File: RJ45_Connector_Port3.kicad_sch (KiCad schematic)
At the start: 8 parts, among them J1 0826-1X4T-43-F

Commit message: Adding page title, and confidential for now
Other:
- title: (none) -> RJ45 Connector Port 3
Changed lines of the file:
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@@
 	(paper "A4")
 	(title_block
+		(title "RJ45 Connector Port 3")
 		(date "2025-12-21")
 		(rev "Rev. A")
 		(company "Kebag-Logic <contact@kebag-logic.com>")
+		(comment 1 "Confidential")
 	)
 	(junction

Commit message: fixes ERC errors in DC/DC converters
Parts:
- C15, C16, C17, C2: footprint Capacitor_SMD:C_0201_0603Metric -> KL_Footprints:C_0603; Dielectric X7R -> (none); Farnell 4539043 -> (none); Package_in_inch 0603 -> (none); Tolerance_in_pct 10 -> (none)
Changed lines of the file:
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@@
 		(dnp no)
 		(property "Reference" "C16"
-			(at 80.01 58.928 90)
-			(effects
-				(font
-					(size 1.27 1.27)
-				)
+			(at 77.47 61.595 0)
+			(effects
+				(font
+					(size 1.27 1.27)
+				)
+				(justify left)
 			)
 		)
 		(property "Value" "100n"
-			(at 80.01 65.786 90)
-			(effects
-				(font
-					(size 1.27 1.27)
-				)
-			)
-		)
-		(property "Footprint" "Capacitor_SMD:C_0201_0603Metric"
+			(at 82.55 61.595 0)
+			(effects
+				(font
+					(size 1.27 1.27)
+				)
+				(justify left)
+			)
+		)
+		(property "Footprint" "KL_Footprints:C_0603"
 			(at 83.82 61.2648 0)
 			(effects
@@
 		)
 		(property "LCSC" "C1591"
-			(at 80.01 62.23 0)
-			(effects
-				(font
-					(size 1.27 1.27)
-				)
-				(hide yes)
-			)
-		)
-		(property "Tolerance_in_pct" "10"
-			(at 80.01 62.23 0)
-			(effects
-				(font
-					(size 1.27 1.27)
-				)
-				(hide yes)
-			)
-		)
-		(property "Dielectric" "X7R"
-			(at 80.01 62.23 0)
-			(effects
-				(font
-					(size 1.27 1.27)
-				)
-				(hide yes)
-			)
-		)
-		(property "Package_in_inch" "0603"
-			(at 80.01 62.23 0)
-			(effects
-				(font
-					(size 1.27 1.27)
-				)
-				(hide yes)
-			)
-		)
-		(property "Farnell" "4539043"
 			(at 80.01 62.23 0)
 			(effects
@@
 		(dnp no)
 		(property "Reference" "C15"
-			(at 80.01 48.514 90)
-			(effects
-				(font
-					(size 1.27 1.27)
-				)
+			(at 77.47 51.435 0)
+			(effects
+				(font
+					(size 1.27 1.27)
+				)
+				(justify left)
 			)
 		)
 		(property "Value" "100n"
-			(at 80.01 55.626 90)
-			(effects
-				(font
-					(size 1.27 1.27)
-				)
-			)
-		)
-		(property "Footprint" "Capacitor_SMD:C_0201_0603Metric"
+			(at 82.55 51.435 0)
+			(effects
+				(font
+					(size 1.27 1.27)
+				)
+				(justify left)
+			)
+		)
+		(property "Footprint" "KL_Footprints:C_0603"
 			(at 83.82 51.1048 0)
 			(effects
@@
 		)
 		(property "LCSC" "C1591"
-			(at 80.01 52.07 0)
-			(effects
-				(font
-					(size 1.27 1.27)
-				)
-				(hide yes)
-			)
-		)
-		(property "Tolerance_in_pct" "10"
-			(at 80.01 52.07 0)
-			(effects
-				(font
-					(size 1.27 1.27)
-				)
-				(hide yes)
-			)
-		)
-		(property "Dielectric" "X7R"
-			(at 80.01 52.07 0)
-			(effects
-				(font
-					(size 1.27 1.27)
-				)
-				(hide yes)
-			)
-		)
-		(property "Package_in_inch" "0603"
-			(at 80.01 52.07 0)
-			(effects
-				(font
-					(size 1.27 1.27)
-				)
-				(hide yes)
-			)
-		)
-		(property "Farnell" "4539043"
 			(at 80.01 52.07 0)
 			(effects
@@
 		(dnp no)
 		(property "Reference" "C17"
-			(at 80.01 68.834 90)
-			(effects
-				(font
-					(size 1.27 1.27)
-				)
+			(at 77.47 71.755 0)
+			(effects
+				(font
+					(size 1.27 1.27)
+				)
+				(justify left)
 			)
 		)
 		(property "Value" "100n"
-			(at 80.01 75.946 90)
-			(effects
-				(font
-					(size 1.27 1.27)
-				)
-			)
-		)
-		(property "Footprint" "Capacitor_SMD:C_0201_0603Metric"
+			(at 82.55 71.755 0)
+			(effects
+				(font
+					(size 1.27 1.27)
+				)
+				(justify left)
+			)
+		)
+		(property "Footprint" "KL_Footprints:C_0603"
 			(at 83.82 71.4248 0)
 			(effects
@@
 		)
 		(property "LCSC" "C1591"
-			(at 80.01 72.39 0)
-			(effects
-				(font
-					(size 1.27 1.27)
-				)
-				(hide yes)
-			)
-		)
-		(property "Tolerance_in_pct" "10"
-			(at 80.01 72.39 0)
-			(effects
-				(font
-					(size 1.27 1.27)
-				)
-				(hide yes)
-			)
-		)
-		(property "Dielectric" "X7R"
-			(at 80.01 72.39 0)
-			(effects
-				(font
-					(size 1.27 1.27)
-				)
-				(hide yes)
-			)
-		)
-		(property "Package_in_inch" "0603"
-			(at 80.01 72.39 0)
-			(effects
-				(font
-					(size 1.27 1.27)
-				)
-				(hide yes)
-			)
-		)
-		(property "Farnell" "4539043"
 			(at 80.01 72.39 0)
 			(effects
@@
 		(dnp no)
 		(property "Reference" "C2"
-			(at 80.01 38.608 90)
-			(effects
-				(font
-					(size 1.27 1.27)
-				)
+			(at 77.47 41.275 0)
+			(effects
+				(font
+					(size 1.27 1.27)
+				)
+				(justify left)
 			)
 		)
 		(property "Value" "100n"
-			(at 80.01 45.212 90)
-			(effects
-				(font
-					(size 1.27 1.27)
-				)
-			)
-		)
-		(property "Footprint" "Capacitor_SMD:C_0201_0603Metric"
+			(at 82.55 41.275 0)
+			(effects
+				(font
+					(size 1.27 1.27)
+				)
+				(justify left)
+			)
+		)
+		(property "Footprint" "KL_Footprints:C_0603"
 			(at 83.82 40.9448 0)
 			(effects
@@
 			(at 80.01 41.91 0)
 			(effects
-				(font
-					(size 1.27 1.27)
-				)
-				(hide yes)
-			)
-		)
-		(property "Tolerance_in_pct" "10"
-			(at 80.01 41.91 0)
-			(effects
-				(font
-					(size 1.27 1.27)
-				)
-				(hide yes)
-			)
-		)
-		(property "Dielectric" "X7R"
-			(at 80.01 41.91 0)
-			(effects
-				(font
-					(size 1.27 1.27)
-				)
-				(hide yes)
-			)
-		)
-		(property "Package_in_inch" "0603"
-			(at 80.01 41.91 0)
-			(effects
-				(font
-					(size 1.27 1.27)
-				)
-				(hide yes)
-			)
-		)
-		(property "Farnell" "4539043"
-			(at 80.01 41.91 0)
-			(effects

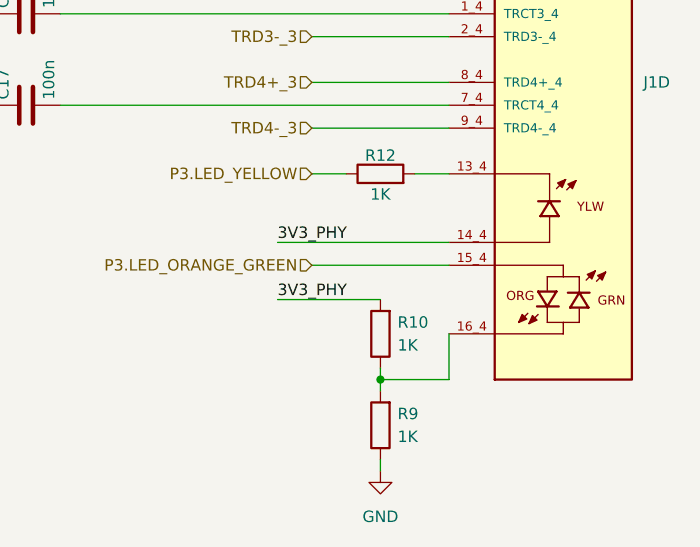
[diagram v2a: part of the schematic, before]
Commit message: updates components from my library misconfiguration. Refs: #1
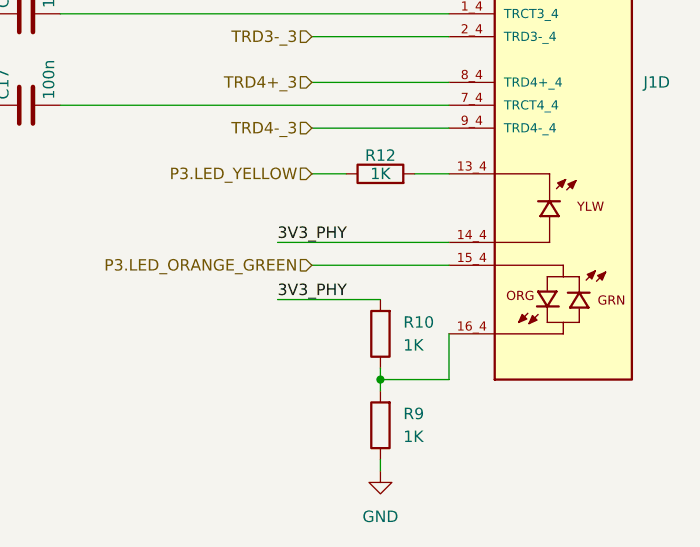
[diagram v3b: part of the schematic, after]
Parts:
- J1: footprint 0826-1X4T-43-F:BEL_0826-1X4T-43-F -> KL_Footprints:BEL_0826-1X4T-43-F
- R10, R12, R9: footprint KL_Footprints:C_0603 -> KL_Footprints:R_0603
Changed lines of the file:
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@@
 		(fields_autoplaced yes)
 		(property "Reference" "R10"
-			(at 121.285 96.5199 0)
+			(at 121.92 96.5199 0)
 			(effects
 				(font
@@
 		)
 		(property "Value" "1K"
-			(at 121.285 99.0599 0)
+			(at 121.92 99.0599 0)
 			(effects
 				(font
@@
 			)
 		)
-		(property "Footprint" "KL_Footprints:C_0603"
+		(property "Footprint" "KL_Footprints:R_0603"
 			(at 121.158 97.79 90)
 			(effects
@@
 			)
 		)
-		(property "Footprint" "0826-1X4T-43-F:BEL_0826-1X4T-43-F"
+		(property "Footprint" "KL_Footprints:BEL_0826-1X4T-43-F"
 			(at 139.7 69.85 0)
 			(effects
@@
 		(fields_autoplaced yes)
 		(property "Reference" "R9"
-			(at 121.285 106.6799 0)
+			(at 121.92 106.6799 0)
 			(effects
 				(font
@@
 		)
 		(property "Value" "1K"
-			(at 121.285 109.2199 0)
+			(at 121.92 109.2199 0)
 			(effects
 				(font
@@
 			)
 		)
-		(property "Footprint" "KL_Footprints:C_0603"
+		(property "Footprint" "KL_Footprints:R_0603"
 			(at 121.158 107.95 90)
 			(effects
@@
 		)
 		(property "Value" "1K"
-			(at 119.38 82.296 90)
-			(effects
-				(font
-					(size 1.27 1.27)
-				)
-			)
-		)
-		(property "Footprint" "KL_Footprints:C_0603"
+			(at 119.38 80.01 90)
+			(effects
+				(font
+					(size 1.27 1.27)
+				)
+			)
+		)
+		(property "Footprint" "KL_Footprints:R_0603"
 			(at 119.38 81.788 90)
 			(effects

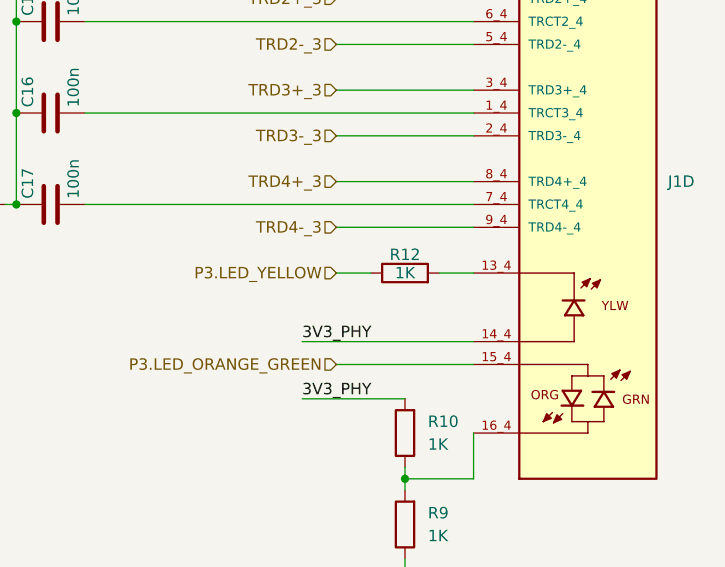
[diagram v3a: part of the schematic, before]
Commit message: removes unused busses, adds cheaper 0R resistor, clean up to fix ERC errors. Refs: #1
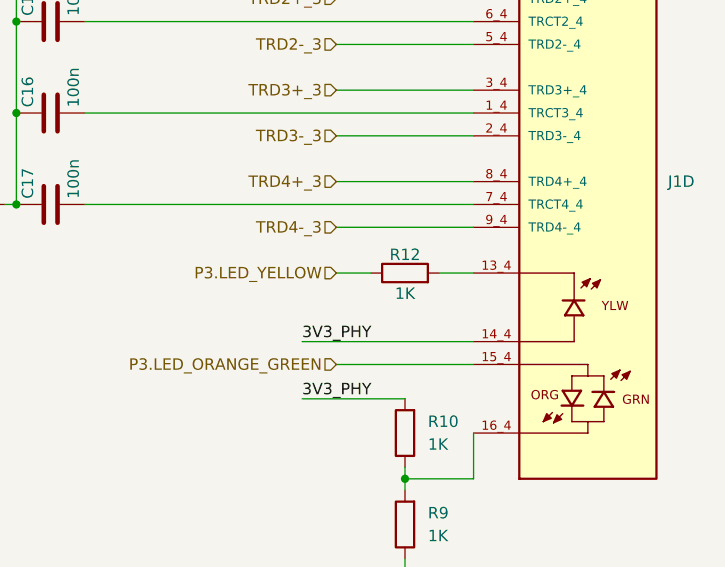
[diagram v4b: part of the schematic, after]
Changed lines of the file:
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@@
 		)
 		(property "Value" "1K"
-			(at 119.38 80.01 90)
+			(at 119.38 82.296 90)
 			(effects
 				(font
